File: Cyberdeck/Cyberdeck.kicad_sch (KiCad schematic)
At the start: 0 parts

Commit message: Imported components for Power Supply
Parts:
- added BAT1: MY-18650-05-J, lcsc_footprints:C19184124_BAT-TH_MY-18650-05-J, symbol lcsc_imported:MY-18650-05-J
- added C1: CL10B105KB8NQNC, lcsc_footprints:C5199872_C0603, symbol lcsc_imported:CL10B105KB8NQNC
- added C2: 4.7uF (475) ±10% 25V, lcsc_footprints:C69335_C0603, symbol lcsc_imported:4_7uF_(475)_±10%_25V
- added LED1: XL-1608SURC-06, lcsc_footprints:C965799_LED0603-RD_RED, symbol lcsc_imported:XL-1608SURC-06
- added LED2: A-SP192DGHC-C01-4T, lcsc_footprints:C19171301_LED0603-FD, symbol lcsc_imported:A-SP192DGHC-C01-4T
- added R1: FRC0603F5100TS, lcsc_footprints:C2907048_R0603, symbol lcsc_imported:FRC0603F5100TS
- added R2: FRC0603F2201TS, lcsc_footprints:C2907005_R0603, symbol lcsc_imported:FRC0603F2201TS
- added R3: FRC0603F3301TS, lcsc_footprints:C2907023_R0603, symbol lcsc_imported:FRC0603F3301TS
- added U1: USB-Friendly Li-Ion Battery Charger and Power-Pat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, lcsc_footprints:C15464_QFN-16_L3_0-W3_0-P0_50-TL-EP1_7, symbol lcsc_imported:USB-Friendly_Li-Ion_Battery_Charger_and_Power-Path_Management_IC,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
- added U2: MY-18650-02, lcsc_footprints:C2979182_BAT-SMD_MY-18650-02, symbol lcsc_imported:MY-18650-02

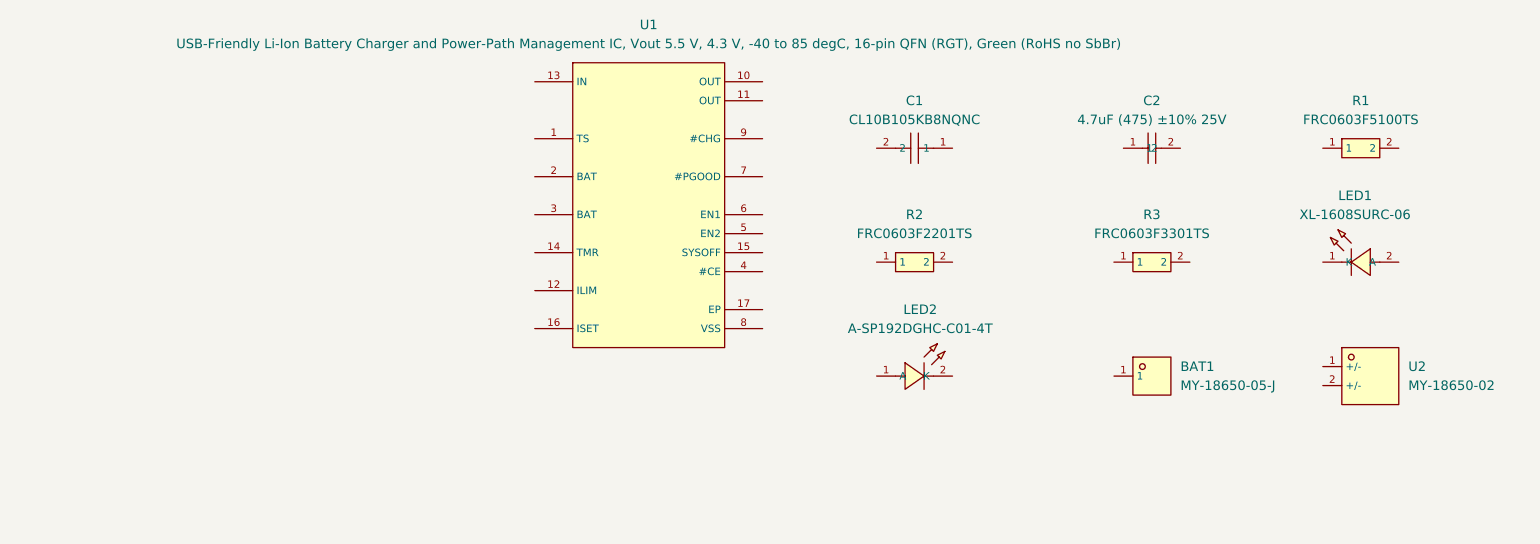
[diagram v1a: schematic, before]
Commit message: Connected battery charger schematic
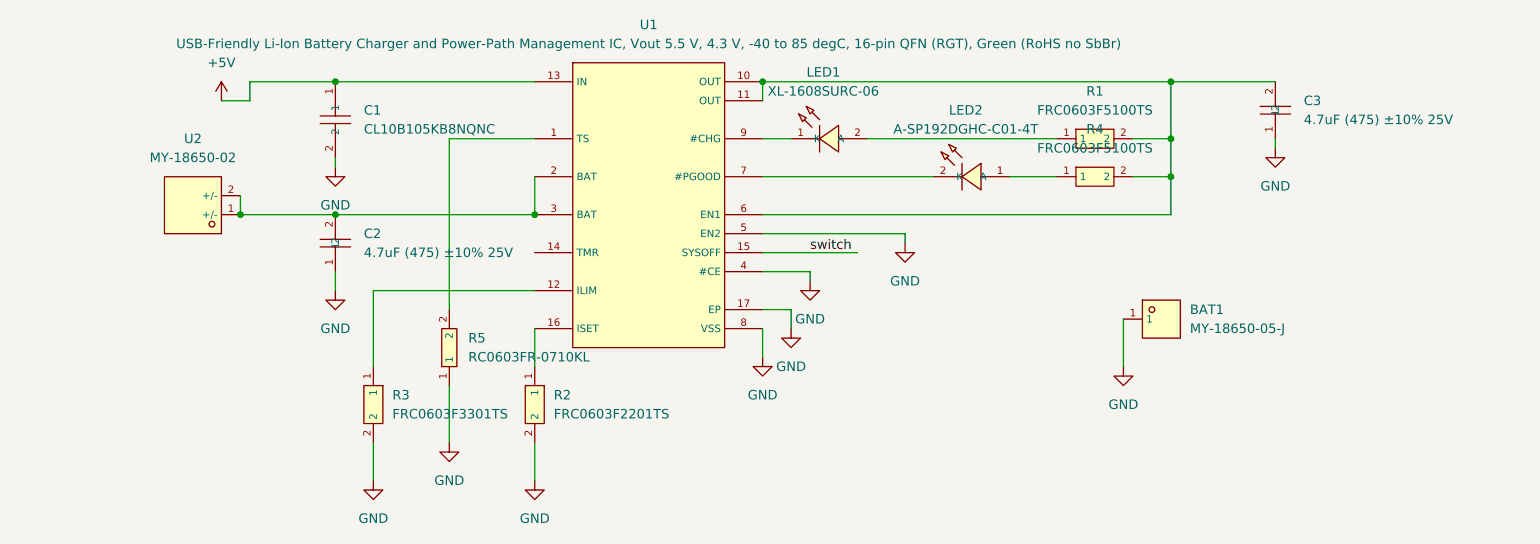
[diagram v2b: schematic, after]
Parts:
- added C3: 4.7uF (475) ±10% 25V, lcsc_footprints:C69335_C0603, symbol lcsc_imported:4_7uF_(475)_±10%_25V
- added R4: FRC0603F5100TS, lcsc_footprints:C2907048_R0603, symbol lcsc_imported:FRC0603F5100TS
- added R5: RC0603FR-0710KL, lcsc_footprints:C98220_R0603, symbol lcsc_imported:RC0603FR-0710KL
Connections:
- net at U2.1 (+/-): now also C2.2, U1.2 (BAT), U1.3 (BAT), U2.2 (+/-)
- net at R3.1: now also U1.12 (ILIM)
- net GND: now reaches R3.2
- net GND: now also BAT1.1, C1.2, C2.1, R2.2, U1.17 (EP), U1.4 (#CE), U1.5 (EN2), U1.8 (VSS), C3.1, R5.1
- net at U1.1 (TS): now also R5.2
- net at U1.10 (OUT): now also R1.2, U1.11 (OUT), U1.6 (EN1), C3.2, R4.2
- net +5V: now reaches U1.13 (IN)
- net +5V: now also C1.1
- net switch: now reaches U1.15 (SYSOFF)
- net at U1.16 (ISET): now also R2.1
- net at U1.7 (#PGOOD): now also LED2.2 (K)
- net at U1.9 (#CHG): now also LED1.1 (K)
- net at LED1.2 (A): now also R1.1
- net at LED2.1 (A): now also R4.1
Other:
- moved on the sheet: BAT1, C1, C2, LED1, LED2, R1, R2, R3, U2

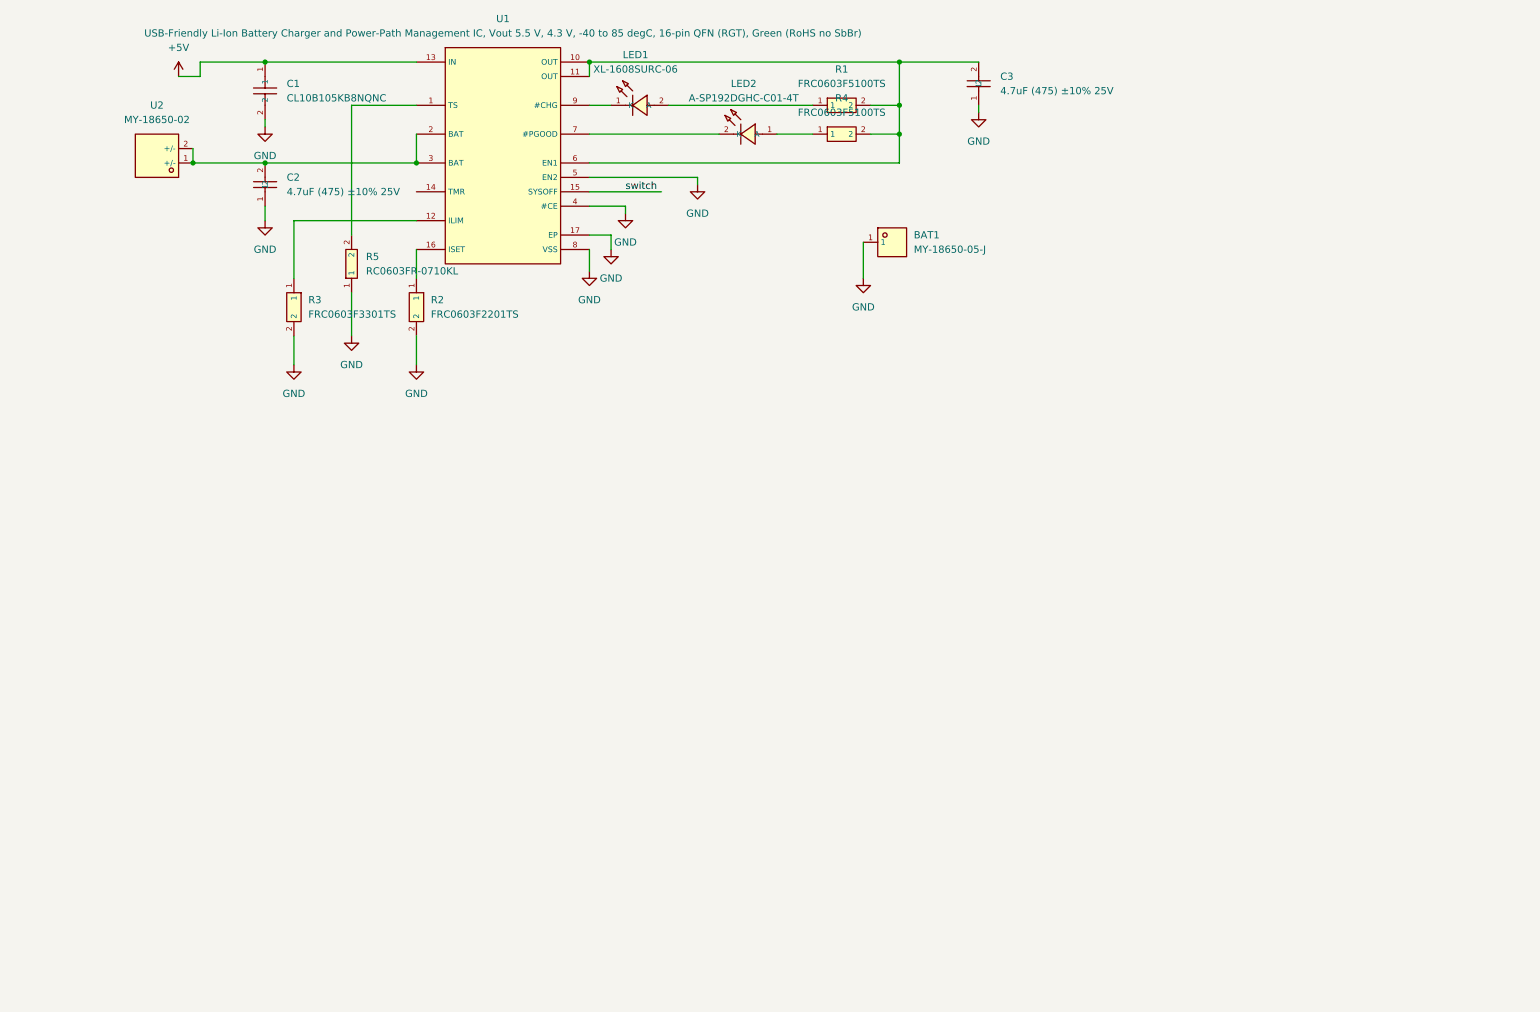
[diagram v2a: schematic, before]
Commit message: Added components for voltage regulator
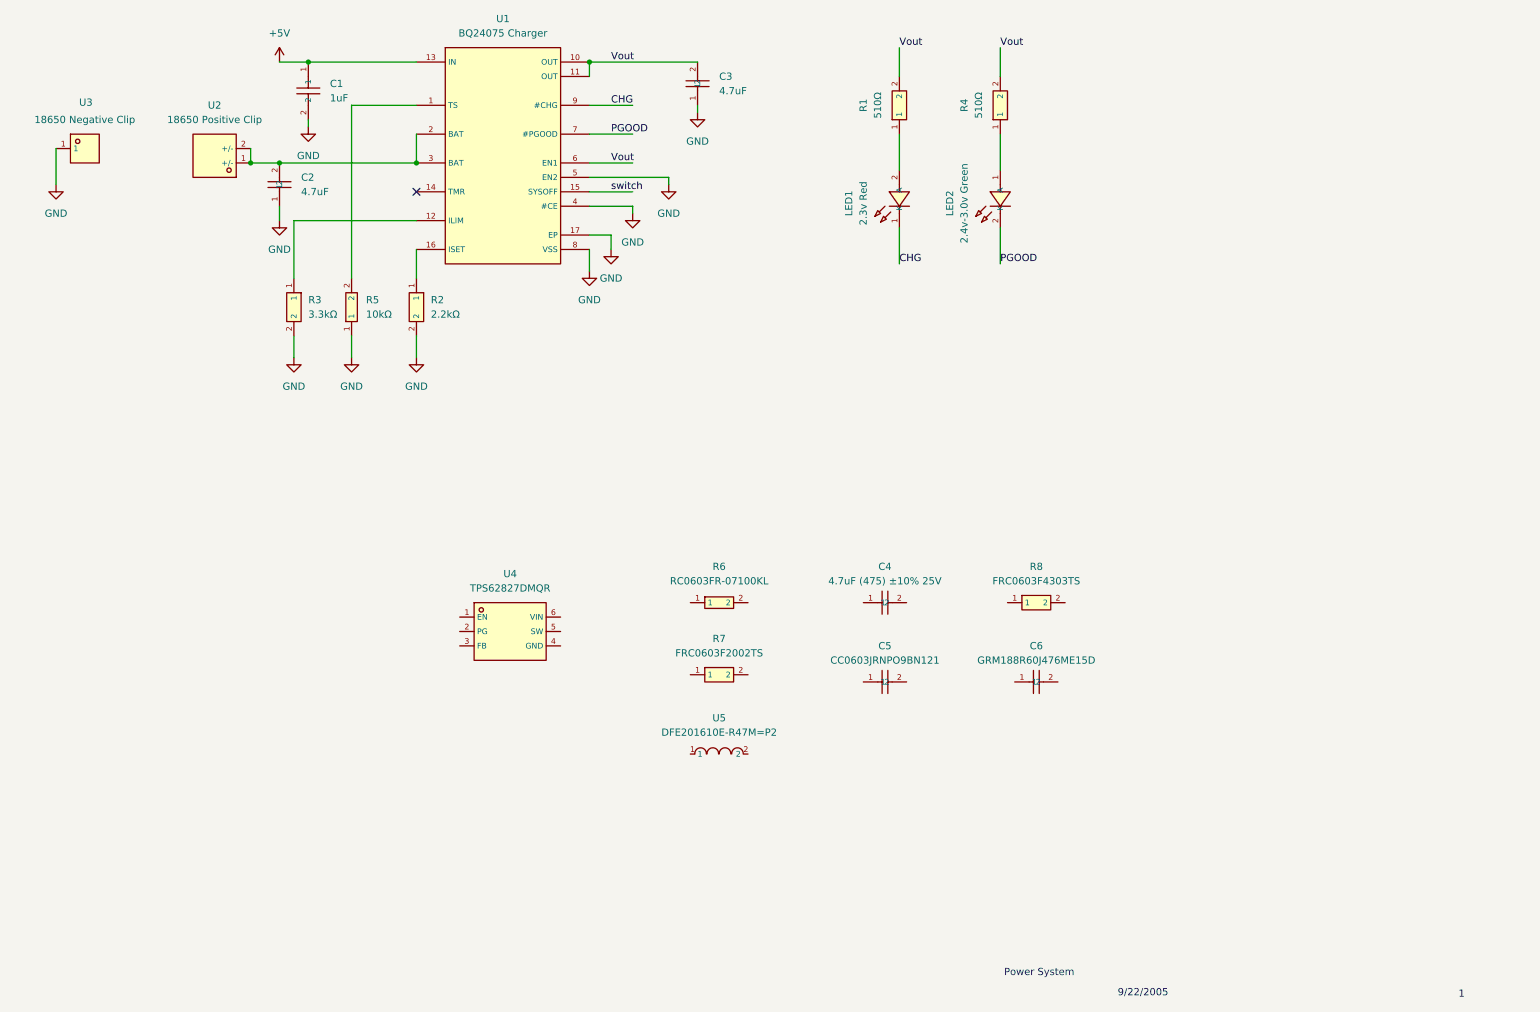
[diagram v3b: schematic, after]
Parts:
- added C4: 4.7uF (475) ±10% 25V, lcsc_footprints:C69335_C0603, symbol lcsc_imported:4_7uF_(475)_±10%_25V
- added C5: CC0603JRNPO9BN121, lcsc_footprints:C107035_C0603, symbol lcsc_imported:CC0603JRNPO9BN121
- added C6: GRM188R60J476ME15D, lcsc_footprints:C140782_C0603, symbol lcsc_imported:GRM188R60J476ME15D
- added R6: RC0603FR-07100KL, lcsc_footprints:C14675_R0603, symbol lcsc_imported:RC0603FR-07100KL
- added R7: FRC0603F2002TS, lcsc_footprints:C2907011_R0603, symbol lcsc_imported:FRC0603F2002TS
- added R8: FRC0603F4303TS, lcsc_footprints:C2907036_R0603, symbol lcsc_imported:FRC0603F4303TS
- added U4: TPS62827DMQR, lcsc_footprints:C2071448_VSON-6_L1_5-W1_5-P0_50-TL, symbol lcsc_imported:TPS62827DMQR
- added U5: DFE201610E-R47M=P2, lcsc_footprints:C269773_L0806, symbol lcsc_imported:DFE201610E-R47M=P2
- C1: value CL10B105KB8NQNC -> 1uF
- C2, C3: value 4.7uF (475) ±10% 25V -> 4.7uF
- LED1: value XL-1608SURC-06 -> 2.3v Red
- LED2: value A-SP192DGHC-C01-4T -> 2.4v-3.0v Green
- R1, R4: value FRC0603F5100TS -> 510Ω
- R2: value FRC0603F2201TS -> 2.2kΩ
- R3: value FRC0603F3301TS -> 3.3kΩ
- R5: value RC0603FR-0710KL -> 10kΩ
- U1: value USB-Friendly Li-Ion Battery Charger and Power-Path Management IC, Vout 5.5 V, 4.3 V, -40 to 85 degC, 16-pin QFN (RGT), 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 -> BQ24075 Charger
- U2: value MY-18650-02 -> 18650 Positive Clip
- U3: renamed from BAT1; value MY-18650-05-J -> 18650 Negative Clip
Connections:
- net Vout: now reaches C3.2, R1.2, R4.2, U1.10 (OUT), U1.11 (OUT), U1.6 (EN1)
- net PGOOD: now reaches LED2.2 (K), U1.7 (#PGOOD)
- net CHG: now reaches LED1.1 (K), U1.9 (#CHG)
- no-connect marks 0 -> 1
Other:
- note added: "1"
- note added: "9/22/2005"
- note added: "Power System"
- moved on the sheet: C1, C2, C3, LED1, LED2, R1, R4, R5, U2, U3

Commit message: Added and populated IO/MCU schematic
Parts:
- removed U3: 18650 Negative Clip, lcsc_footprints:C19184124_BAT-TH_MY-18650-05-J, symbol lcsc_imported:MY-18650-05-J
- added BAT1: MY-18650-05-J, lcsc_footprints:C19184124_BAT-TH_MY-18650-05-J, symbol lcsc_imported:MY-18650-05-J
- added R9: 100kΩ, lcsc_footprints:C14675_R0603, symbol lcsc_imported:RC0603FR-07100KL
- C4: value 4.7uF (475) ±10% 25V -> 4.7uF
- C5: value CC0603JRNPO9BN121 -> 120pF
- C6: value GRM188R60J476ME15D -> 47uF
- R6: value RC0603FR-07100KL -> 100kΩ
- R7: value FRC0603F2002TS -> 20kΩ
- R8: value FRC0603F4303TS -> 430kΩ
- U4: value TPS62827DMQR -> TPS62827 Regulator
- U5: value DFE201610E-R47M=P2 -> 0.47uH
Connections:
- net Vout is gone; now on net V_CHG: C3.2, R1.2, R4.2, U1.10 (OUT), U1.11 (OUT), U1.6 (EN1)
- net GND: now also C4.2, C6.2, U4.4 (GND), BAT1.1, R9.2
- net V_OUT: now reaches U5.1
- net V_OUT: now also C5.1, C6.1, R8.2
- net at U5.2: now also U4.5 (SW)
- net V_CHG: now reaches C4.1
- net V_CHG: now also R6.1, U4.1 (EN), U4.6 (VIN)
- net at U4.2 (PG): now also R6.2
- net at U4.3 (FB): now also C5.2, R7.1, R9.1
- net at R8.1: now also R7.2
- net +5V renamed V_IN
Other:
- added sheet IOConfig (IOConfig.kicad_sch)
- added sheet MicroController (MicroController.kicad_sch)
- moved on the sheet: C4, C5, C6, R6, R7, R8, U5

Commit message: Finished schematic
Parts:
- added SW1: Slide Switch, lcsc_footprints:C2939726_SW-TH_SS12D07VG4, symbol lcsc_imported:SS12D07VG4_087
- BAT1: value MY-18650-05-J -> 18650 Neg Clip
- renumbered C3 to C1, C1 to C2, C2 to C3, C6 to C5, C5 to C6, R4 to R2, R5 to R4, R2 to R5, R8 to R7, R7 to R8, U2 to U1, U1 to U2, U5 to U3
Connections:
- net GND: now also SW1.3
- net V_CHG: no longer U4.1 (EN)
- net V_BAT: now reaches C3.2, U1.1 (+/-), U1.2 (+/-), U2.2 (BAT), U2.3 (BAT)
- net V_BAT: now also SW1.1
- net switch renamed Switch
- net Switch: now also U4.1 (EN), SW1.2
- no-connect marks 1 -> 9
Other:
- sheet IOConfig ports: added Backlight, PA2, PA3, PA4, PA5, PA6, PA7, PA8, PB1, PB10, PB12, PB13, PB14, PB15, PB3, PB4, PB5, PB6, PB7, PB8, PB9, V_IN; removed none
- sheet MicroController ports: added PA0, PA10, PA15, PA2, PA3, PA4, PA5, PA6, PA7, PA8, PB0, PB1, PB10, PB12, PB13, PB14, PB15, PB3, PB4, PB5, PB6, PB7, PB8, PB9, PC13, V_IN, V_OUT; removed none
- note added: "9/22/2026"
- note removed: "9/22/2005"
- moved on the sheet: BAT1

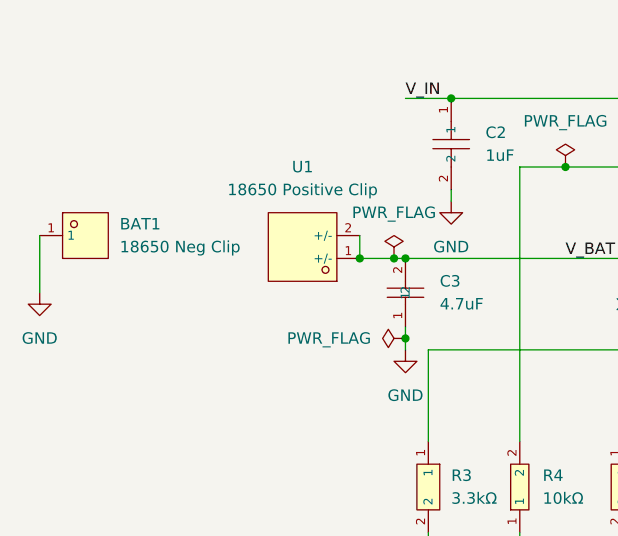
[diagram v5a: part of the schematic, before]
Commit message: Optimized component placement
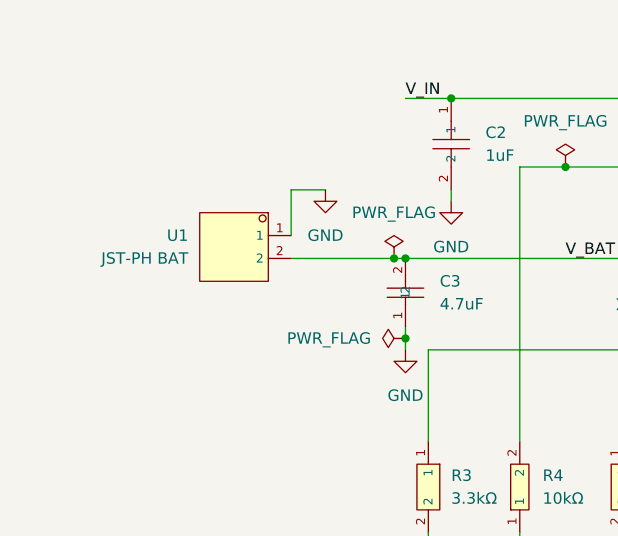
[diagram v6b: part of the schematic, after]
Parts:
- removed BAT1: 18650 Neg Clip, lcsc_footprints:C19184124_BAT-TH_MY-18650-05-J, symbol lcsc_imported:MY-18650-05-J
- removed U1: 18650 Positive Clip, lcsc_footprints:C2979182_BAT-SMD_MY-18650-02, symbol lcsc_imported:MY-18650-02
- added U1: JST-PH BAT, lcsc_footprints:C173752_CONN-TH_S2B-PH-K-S-LF-SN, symbol lcsc_imported:S2B-PH-K-S(LF)(SN)
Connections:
- net GND: now also U1.1
- net V_BAT: now also U1.2

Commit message: Rerouted vias, optimized layout, and added pwr/gnd planes
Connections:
- net GND: now also SW1.4, SW1.5
- net V_IN renamed V_USB
- net V_OUT renamed V_REG
- no-connect marks 9 -> 7
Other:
- sheet IOConfig ports: added V_REG; removed V_IN
- sheet MicroController ports: added V_REG, V_USB; removed V_IN, V_OUT
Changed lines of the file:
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@@
 	)
 	(no_connect
-		(at 240.03 40.64)
-	)
-	(no_connect
 		(at 270.51 138.43)
 	)
@@
 	)
 	(no_connect
-		(at 224.79 40.64)
-	)
-	(no_connect
 		(at 270.51 72.39)
 	)
@@
 	(wire
 		(pts
+			(xy 224.79 40.64) (xy 220.98 40.64)
+		)
+		(stroke
+			(width 0)
+			(type default)
+		)
+	)
+	(wire
+		(pts
 			(xy 63.5 77.47) (xy 63.5 81.28)
 		)
@@
 	(wire
 		(pts
+			(xy 240.03 40.64) (xy 243.84 40.64)
+		)
+		(stroke
+			(width 0)
+			(type default)
+		)
+	)
+	(wire
+		(pts
 			(xy 194.31 116.84) (xy 200.66 116.84)
 		)
@@
 	(wire
 		(pts
+			(xy 243.84 40.64) (xy 243.84 41.91)
+		)
+		(stroke
+			(width 0)
+			(type default)
+		)
+	)
+	(wire
+		(pts
 			(xy 194.31 106.68) (xy 200.66 106.68)
 		)
@@
 		)
 	)
-	(label "V_OUT"
+	(wire
+		(pts
+			(xy 220.98 40.64) (xy 220.98 41.91)
+		)
+		(stroke
+			(width 0)
+			(type default)
+		)
+	)
+	(label "V_REG"
 		(at 220.98 71.12 0)
 		(effects
@@
 		)
 	)
-	(label "V_IN"
+	(label "V_USB"
 		(at 60.96 29.21 0)
 		(effects
@@
 		)
 	)
-	(label "V_IN"
+	(label "V_USB"
 		(at 220.98 74.93 0)
 		(effects
@@
 		)
 	)
-	(label "V_OUT"
+	(label "V_REG"
 		(at 35.56 129.54 0)
 		(effects
@@
 		)
 	)
-	(label "V_OUT"
+	(label "V_REG"
 		(at 160.02 86.36 0)
 		(effects
@@
 	(symbol
 		(lib_id "power:GND")
+		(at 220.98 41.91 0)
+		(unit 1)
+		(body_style 1)
+		(exclude_from_sim no)
+		(in_bom yes)
+		(on_board yes)
+		(in_pos_files yes)
+		(dnp no)
+		(fields_autoplaced yes)
+		(property "Reference" "#PWR054"
+			(at 220.98 48.26 0)
+			(hide yes)
+			(show_name no)
+			(do_not_autoplace no)
+			(effects
+				(font
+					(size 1.27 1.27)
+				)
+			)
+		)
+		(property "Value" "GND"
+			(at 220.98 46.99 0)
+			(show_name no)
+			(do_not_autoplace no)
+			(effects
+				(font
+					(size 1.27 1.27)
+				)
+			)
+		)
+		(property "Footprint" ""
+			(at 220.98 41.91 0)
+			(hide yes)
+			(show_name no)
+			(do_not_autoplace no)
+			(effects
+				(font
+					(size 1.27 1.27)
+				)
+			)
+		)
+		(property "Datasheet" ""
+			(at 220.98 41.91 0)
+			(hide yes)
+			(show_name no)
+			(do_not_autoplace no)
+			(effects
+				(font
+					(size 1.27 1.27)
+				)
+			)
+		)
+		(property "Description" "Power symbol creates a global label with name \"GND\" , ground"
+			(at 220.98 41.91 0)
+			(hide yes)
+			(show_name no)
+			(do_not_autoplace no)
+			(effects
+				(font
+					(size 1.27 1.27)
+				)
+			)
+		)
+		(pin "1"
+		)
+		(instances
+			(project "Cyberdeck"
+				(path "/8993e48e-9b31-4221-b933-aeda00ea11c8"
+					(reference "#PWR054")
+					(unit 1)
+				)
+			)
+		)
+	)
+	(symbol
+		(lib_id "power:GND")
 		(at 129.54 50.8 0)
 		(unit 1)
@@
 	)
 	(symbol
+		(lib_id "power:GND")
+		(at 243.84 41.91 0)
+		(unit 1)
+		(body_style 1)
+		(exclude_from_sim no)
+		(in_bom yes)
+		(on_board yes)
+		(in_pos_files yes)
+		(dnp no)
+		(fields_autoplaced yes)
+		(property "Reference" "#PWR04"
+			(at 243.84 48.26 0)
+			(hide yes)
+			(show_name no)
+			(do_not_autoplace no)
+			(effects
+				(font
+					(size 1.27 1.27)
+				)
+			)
+		)
+		(property "Value" "GND"
+			(at 243.84 46.99 0)
+			(show_name no)
+			(do_not_autoplace no)
+			(effects
+				(font
+					(size 1.27 1.27)
+				)
+			)
+		)
+		(property "Footprint" ""
+			(at 243.84 41.91 0)
+			(hide yes)
+			(show_name no)
+			(do_not_autoplace no)
+			(effects
+				(font
+					(size 1.27 1.27)
+				)
+			)
+		)
+		(property "Datasheet" ""
+			(at 243.84 41.91 0)
+			(hide yes)
+			(show_name no)
+			(do_not_autoplace no)
+			(effects
+				(font
+					(size 1.27 1.27)
+				)
+			)
+		)
+		(property "Description" "Power symbol creates a global label with name \"GND\" , ground"
+			(at 243.84 41.91 0)
+			(hide yes)
+			(show_name no)
+			(do_not_autoplace no)
+			(effects
+				(font
+					(size 1.27 1.27)
+				)
+			)
+		)
+		(pin "1"
+		)
+		(instances
+			(project "Cyberdeck"
+				(path "/8993e48e-9b31-4221-b933-aeda00ea11c8"
+					(reference "#PWR04")
+					(unit 1)
+				)
+			)
+		)
+	)
+	(symbol
 		(lib_id "power:PWR_FLAG")
 		(at 78.74 154.94 0)
@@
 			)
 		)
-		(pin "V_IN" input
+		(pin "V_REG" input
 			(at 228.6 71.12 180)
 			(effects
@@
 			)
 		)
-		(pin "V_OUT" output
+		(pin "V_USB" output
 			(at 228.6 74.93 180)
 			(effects
@@
 			)
 		)
-		(pin "V_IN" input
-			(at 166.37 86.36 180)
+		(pin "Backlight" bidirectional
+			(at 166.37 90.17 180)
 			(effects
 				(font
@@
 			)
 		)
-		(pin "Backlight" bidirectional
-			(at 166.37 90.17 180)
+		(pin "V_REG" input
+			(at 166.37 86.36 180)
 			(effects
 				(font
